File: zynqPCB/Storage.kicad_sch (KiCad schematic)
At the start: 22 parts, among them J8 Micro_SD_Card_Det, U17 FTDITypeUART, U18 ABRACON-ASDMB, U19 S25FL256SAGNFI001, U20F xc7z020clg484

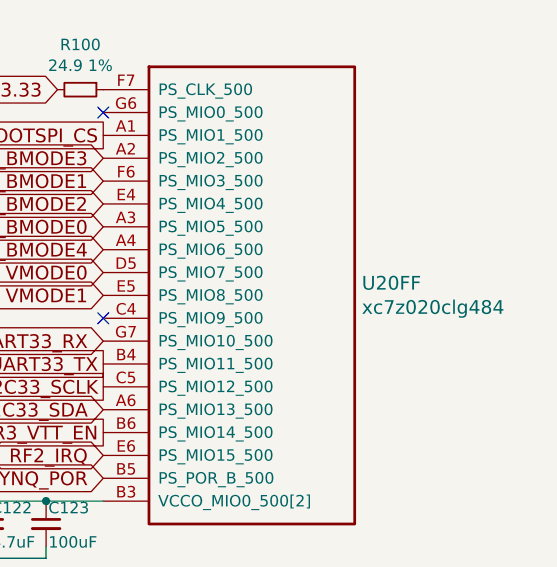
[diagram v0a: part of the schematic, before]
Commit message: Update audio schematic
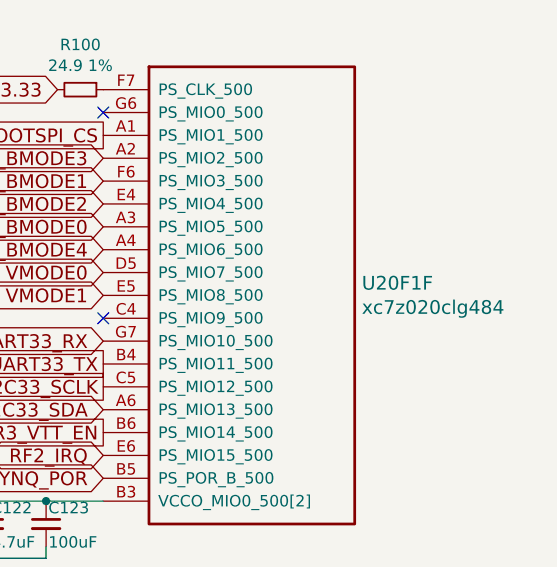
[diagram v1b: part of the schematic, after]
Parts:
- renumbered U20F to U20F1
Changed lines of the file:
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@@
 		(on_board yes)
 		(dnp no)
-		(property "Reference" "U20F"
+		(property "Reference" "U20F1"
 			(at 235.7374 83.7438 0)
 			(effects
@@
 			(project "DFTBoard"
 				(path "/49eba173-d38c-4d05-b21c-b4a14c4948c2/00000000-0000-0000-0000-00005ca1abae"
-					(reference "U20F")
+					(reference "U20F1")
 					(unit 6)
 				)
